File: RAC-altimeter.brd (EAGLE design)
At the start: 25.4 x 50.8 mm, 28 parts, among them J3 CORTEX_DEBUG_SMD, U1 MAX32660GTP+, U2 BMI088, U3 BMP388, U4 W25N01GVZEIG_TR, Y1 32.768kHz

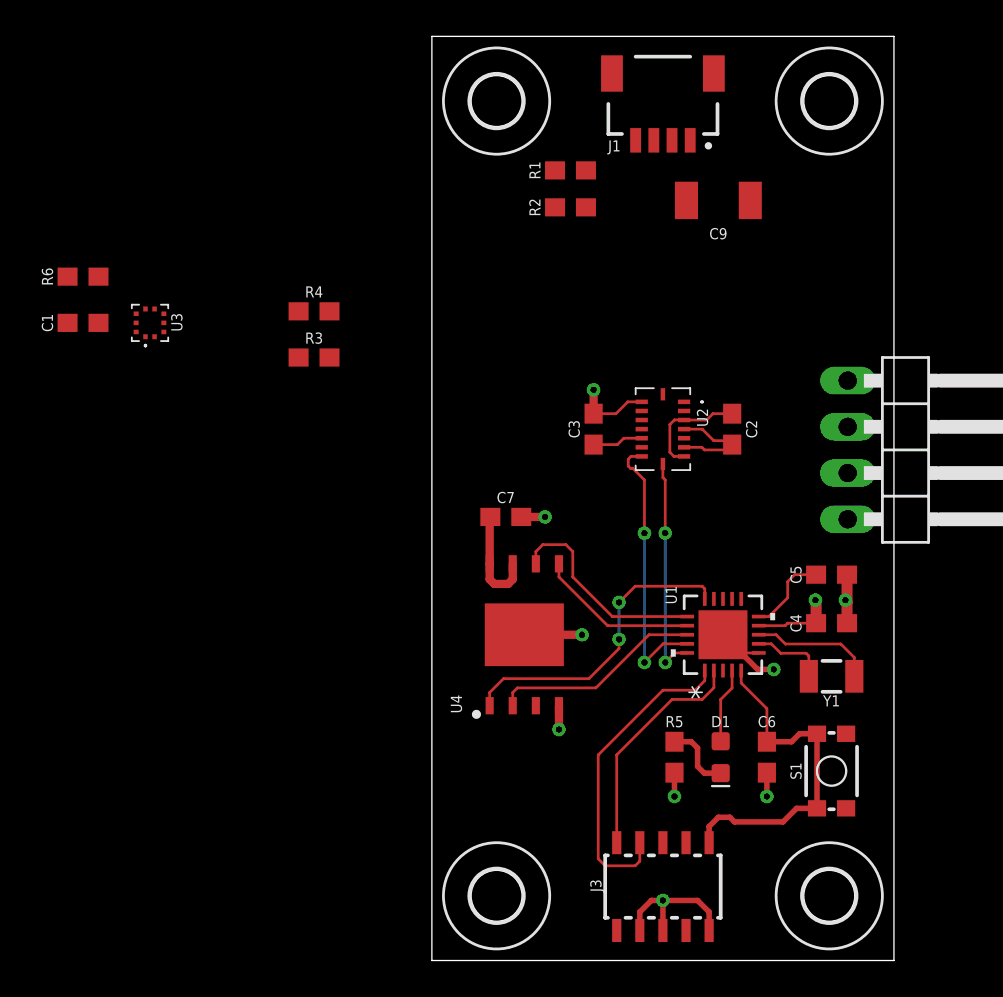
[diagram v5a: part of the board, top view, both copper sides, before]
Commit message: Finished routing board, cleared DRC
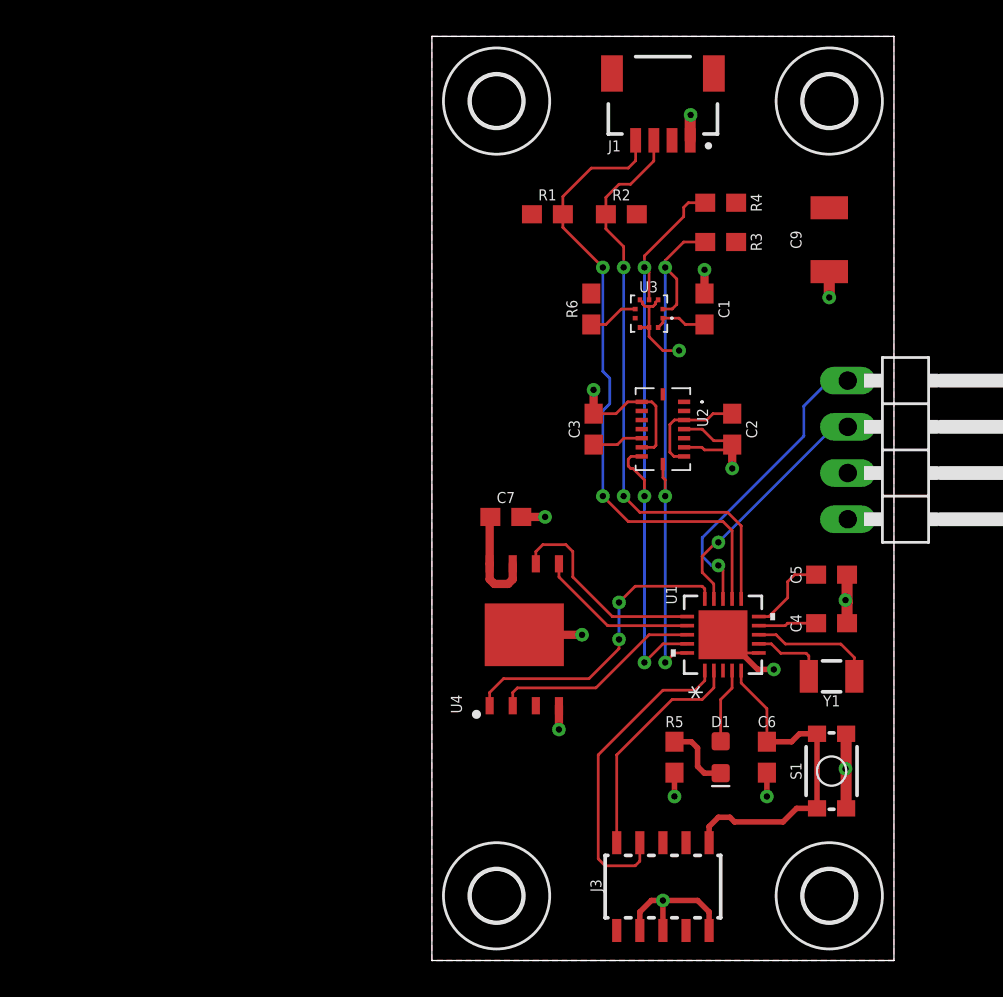
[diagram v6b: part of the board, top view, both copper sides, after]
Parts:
- moved C1 34.2 mm to (15.0, 35.8), turned to 90 degrees
- moved R6 28.0 mm to (8.76, 35.8), turned to 90 degrees
- moved U3 27.4 mm to (11.9, 35.6), turned to 270 degrees
- moved R3 23.2 mm to (15.9, 39.5)
- moved R4 23.1 mm to (15.9, 41.7), turned to 0 degrees
- moved C9 6.47 mm to (21.8, 39.6), turned to 270 degrees
- moved R2 2.82 mm to (10.4, 41.0), turned to 0 degrees
- moved R1 2.73 mm to (6.35, 41.0)
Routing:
- net I2C0_SCL: track 0.00 -> 35.3 mm, vias 0 -> 2
- net I2C0_SDA: track 0.00 -> 32.6 mm, vias 0 -> 2
- net I2C1_SDA: track 15.2 -> 35.1 mm, vias 2 -> 3
- net GND: track 35.2 -> 54.2 mm, vias 9 -> 15
- net I2C1_SCL: track 12.4 -> 31.1 mm, vias 2 -> 3
- net UART1_RX: track 0.00 -> 16.6 mm, vias 0 -> 1
- net UART1_TX: track 0.00 -> 13.6 mm, vias 0 -> 1
- net BMP_CS: track 0.00 -> 2.76 mm
- net VCC: track 19.1 -> 20.9 mm, vias 1 -> 0
- added copper zone on layer 16, net GND
- added copper zone on layer 1, net VCC
